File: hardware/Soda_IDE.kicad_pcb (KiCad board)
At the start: 2 copper layers, 101.6 x 65.5 mm, 25 parts, among them CN1 MSX_SLOT_CON, J2 Conn_CF_Card, J3 Conn_02x22_Odd_Even, Q1 BC548, SW1 SW_Push, SW2 SW_Push_SPDT, U1 27C512, U2 74HCT74, U3 74LS32, U4 74HCT138

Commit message: fixes and updates
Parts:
- added JP2: SolderJumper_2_Open, Jumper:SolderJumper-2_P1.3mm_Open_RoundedPad1.0x1.5mm, F.Cu at (186.1, 105.4)
- added JP3: SolderJumper_2_Open, Jumper:SolderJumper-2_P1.3mm_Open_RoundedPad1.0x1.5mm, F.Cu at (190.5, 105.4)
- added JP4: SolderJumper_2_Open, Jumper:SolderJumper-2_P1.3mm_Open_RoundedPad1.0x1.5mm, F.Cu at (194.9, 105.4)
- U2: renamed from U3; value 74LS32 -> 74HCT32
- renumbered C3 to C2, C2 to C3, D2 to D1, J3 to J1, JP2 to J2, J2 to J3, D1 to LD1, R6 to R1, R4 to R2, R5 to R3, R2 to R4, R1 to R5, R3 to R6, U2 to U3
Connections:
- J3 pad 7: /~{SEL} -> /~{IDE_CS0}
- U3 pad 13: /IORQ -> /~{IORQ}
- U4 pad 12: unconnected-(U4-~{Y3}-Pad12) -> Net-(JP2-A)
- U4 pad 13: /~{IDE_CS0} -> Net-(JP3-A)
- U4 pad 15: unconnected-(U4-~{Y0}-Pad15) -> Net-(JP4-A)
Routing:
- net /~{IORQ}: track 0.00 -> 51.4 mm, vias 0 -> 1
- net /~{IDE_CS0}: track 97.2 -> 144.3 mm, vias 1 -> 2
- net Net-(JP4-A): track 0.00 -> 11.5 mm
- net Net-(JP3-A): track 0.00 -> 11.3 mm
- net Net-(JP2-A): track 0.00 -> 10.7 mm
- net /CLOCK: track 100.6 -> 106.2 mm
- net Net-(D1-K): track 64.5 -> 66.6 mm
- net Net-(Q1-B): track 7.30 -> 5.80 mm
- net /D7: track 105.5 -> 106.0 mm
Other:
- board text added: "10h"
- board text added: "30h"
- board text added: "38h"
- board text added: "PCB by Danjovic FW by b3rendsh October 2024"
- board text added: "Z80 RESET"
- board text removed: "Danjovic 2024"

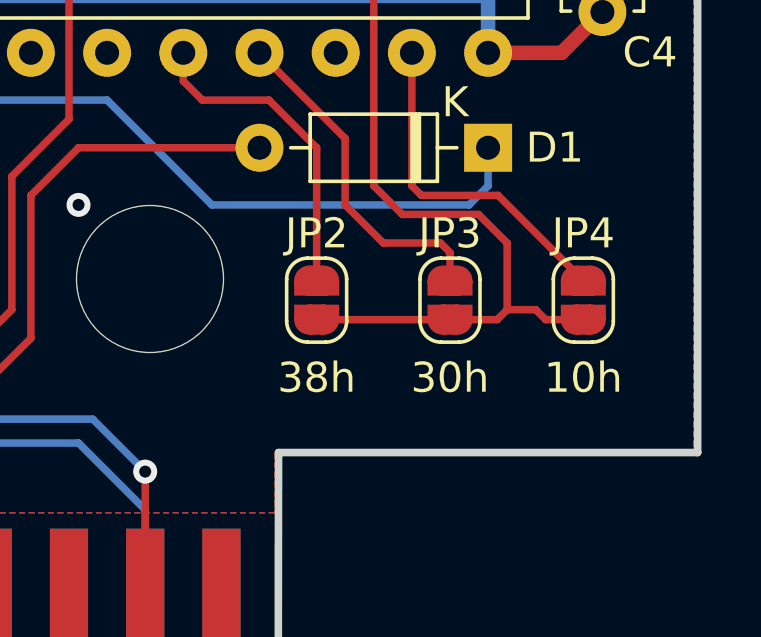
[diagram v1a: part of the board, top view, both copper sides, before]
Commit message: conventional jumpers for address selection
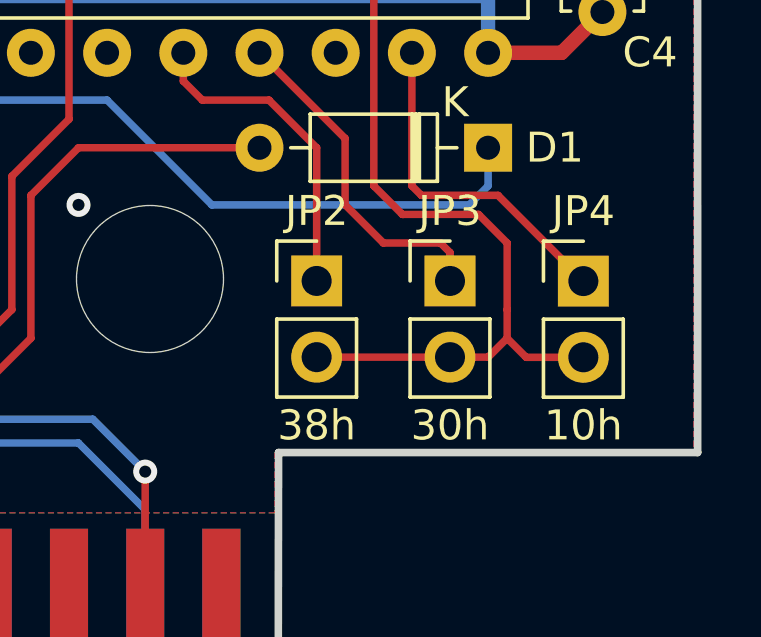
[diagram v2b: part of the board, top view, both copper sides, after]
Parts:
- JP2, JP3, JP4: value SolderJumper_2_Open -> Jumper_2_Small_Open; footprint Jumper:SolderJumper-2_P1.3mm_Open_RoundedPad1.0x1.5mm -> Connector_PinHeader_2.54mm:PinHeader_1x02_P2.54mm_Vertical
- moved JP2 0.64 mm to (186.1, 104.8), turned to 0 degrees
- moved JP3 0.64 mm to (190.5, 104.8), turned to 0 degrees
- moved JP4 0.63 mm to (194.9, 104.8), turned to 0 degrees
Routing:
- net /~{IDE_CS0}: track 144.3 -> 145.5 mm

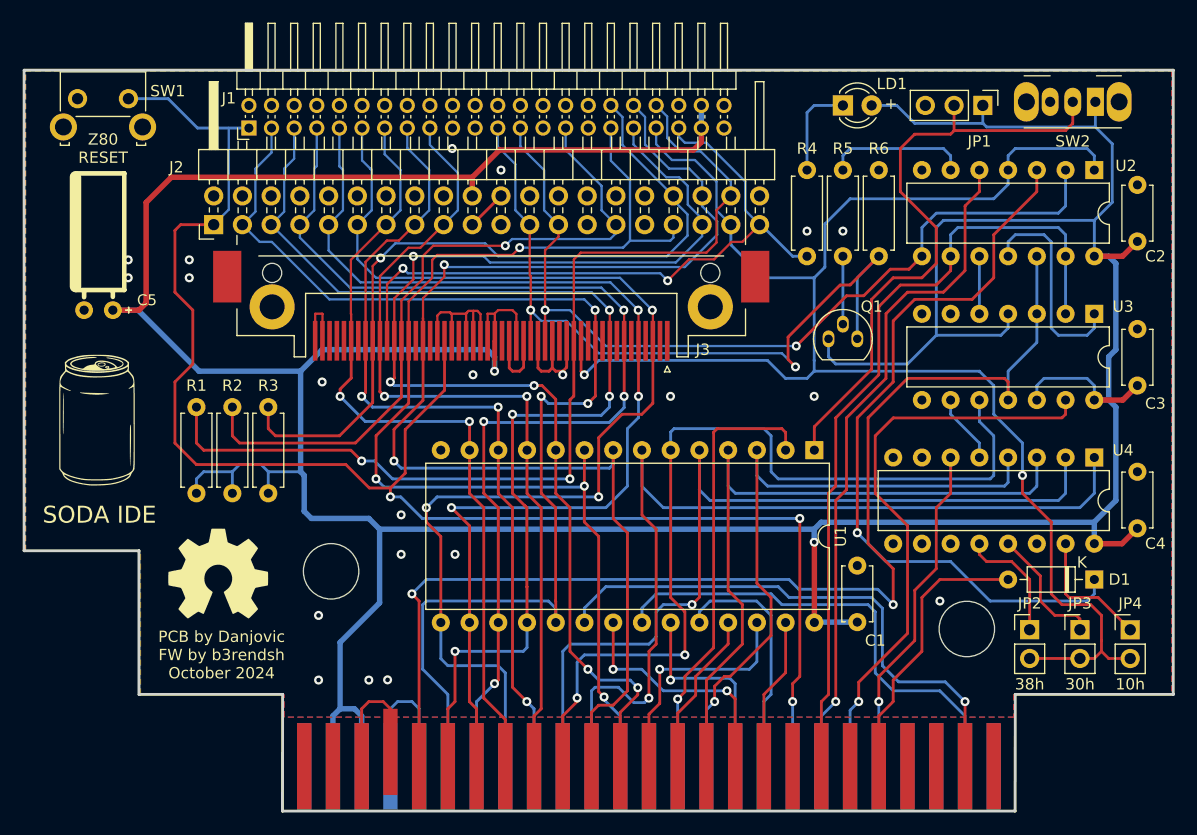
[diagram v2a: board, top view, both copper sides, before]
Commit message: Added buffer to data lines
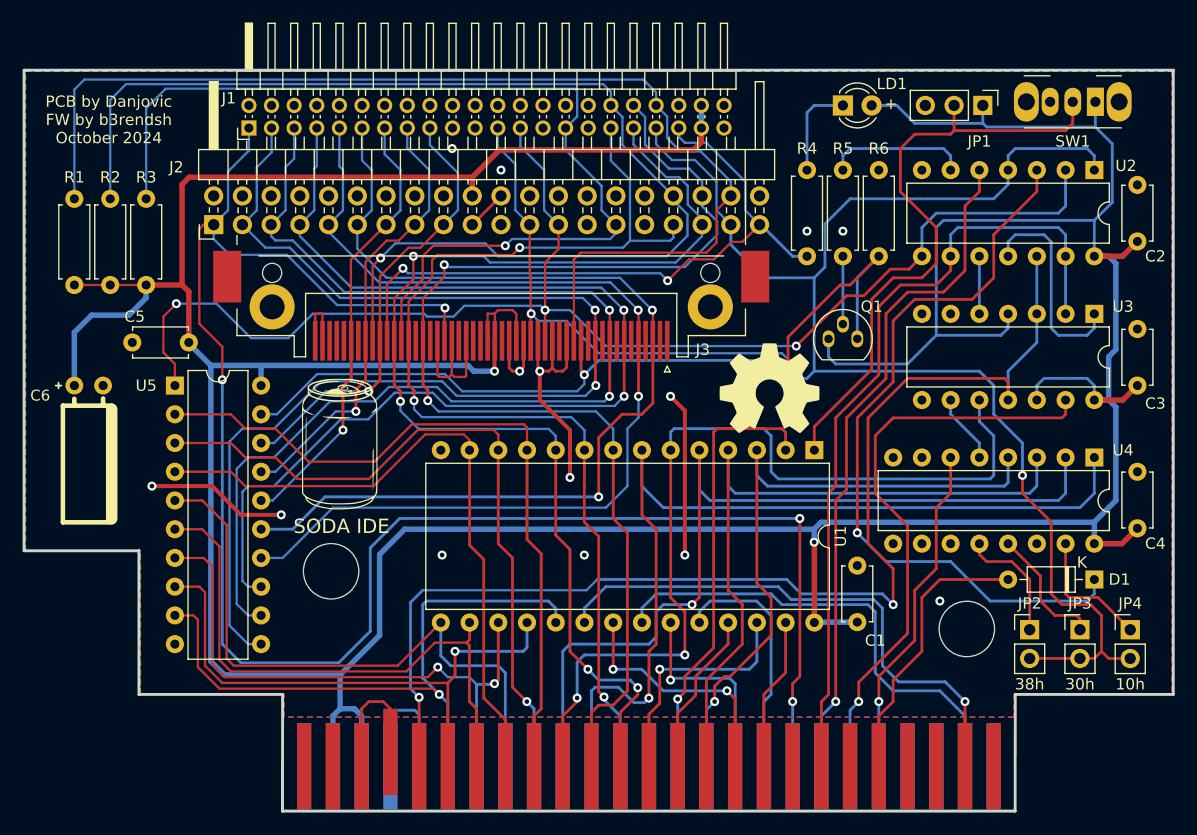
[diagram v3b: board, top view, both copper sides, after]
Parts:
- removed the SW1 at (101.9, 57.8)
- added C5: 100nF, Capacitor_THT:C_Disc_D4.7mm_W2.5mm_P5.00mm, F.Cu at (111.7, 79.4)
- added U5: 74HC245, Package_DIP:DIP-20_W7.62mm, F.Cu at (110.5, 83.2)
- moved R2 23.1 mm to (104.8, 66.7)
- moved R1 21.3 mm to (101.6, 66.7)
- moved R3 19.9 mm to (108.0, 66.7)
- moved C6 6.72 mm to (102.9, 83.2), turned to 0 degrees
- renumbered C5 to C6, R3 to R2, R2 to R3, SW2 to SW1
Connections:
- CN1 pad 33: /D1 -> /zD1
- CN1 pad 34: /D0 -> /zD0
- CN1 pad 35: /D3 -> /zD3
- CN1 pad 36: /D2 -> /zD2
- CN1 pad 37: /D5 -> /zD5
- CN1 pad 38: /D4 -> /zD4
- CN1 pad 39: /D7 -> /zD7
- CN1 pad 40: /D6 -> /zD6
- U1 pad 11: /D0 -> /zD0
- U1 pad 12: /D1 -> /zD1
- U1 pad 13: /D2 -> /zD2
- U1 pad 15: /D3 -> /zD3
- U1 pad 16: /D4 -> /zD4
- U1 pad 17: /D5 -> /zD5
- U1 pad 18: /D6 -> /zD6
- U1 pad 19: /D7 -> /zD7
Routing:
- net /zD0: track 0.00 -> 65.1 mm
- net /zD1: track 0.00 -> 62.5 mm, vias 0 -> 1
- net /zD2: track 0.00 -> 58.8 mm
- net /zD7: track 0.00 -> 57.3 mm, vias 0 -> 1
- net /zD3: track 0.00 -> 55.6 mm
- net /zD5: track 0.00 -> 51.5 mm, vias 0 -> 2
- net /zD4: track 0.00 -> 51.1 mm
- net /zD6: track 0.00 -> 50.6 mm, vias 0 -> 1
- net /~{IORD}: track 77.8 -> 121.4 mm, vias 2 -> 3
- net /PDIAG: track 68.9 -> 105.9 mm
- net /D0: track 74.5 -> 39.6 mm, vias 2 -> 1
- net /D1: track 73.1 -> 39.7 mm, vias 3 -> 1
- net GND: track 55.0 -> 86.9 mm, vias 21 -> 15
- net /~{IDE_CS0}: track 145.5 -> 177.2 mm
- net /D2: track 70.7 -> 39.2 mm, vias 2 -> 1
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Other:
- board text removed: "Z80 RESET"

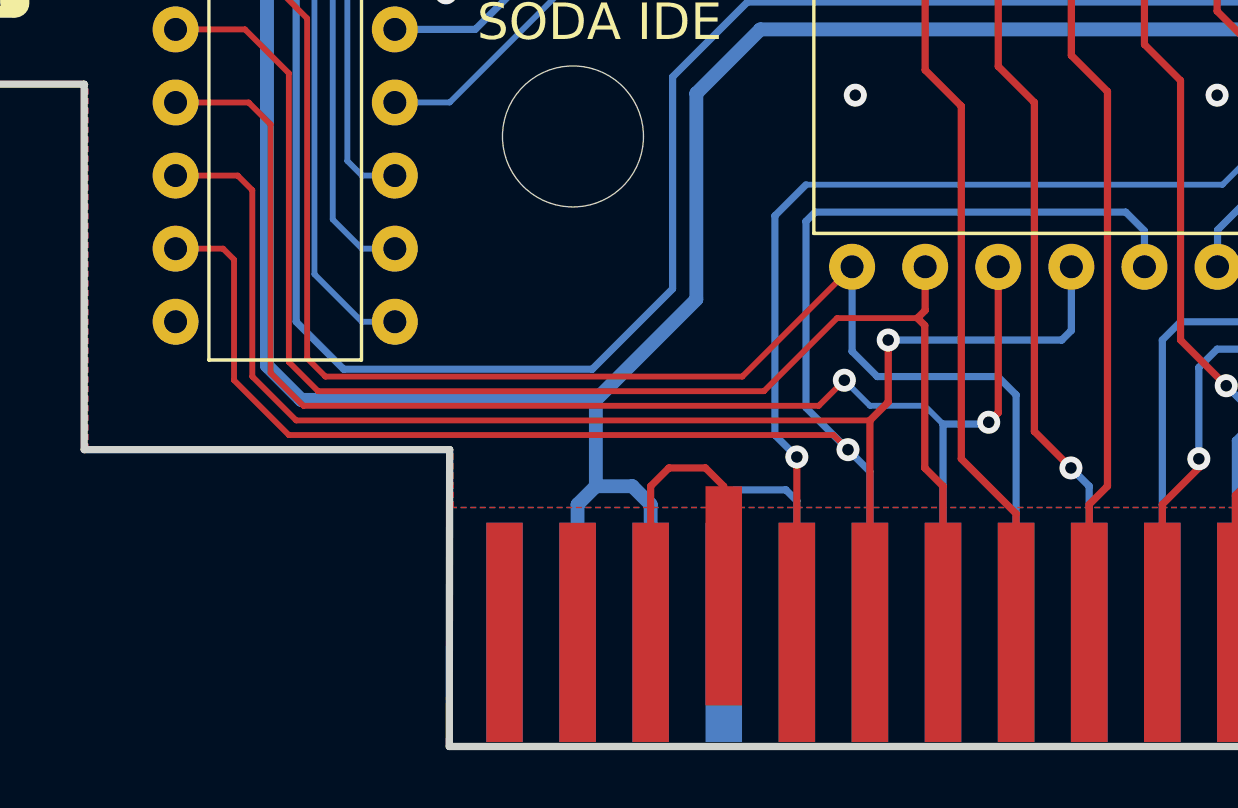
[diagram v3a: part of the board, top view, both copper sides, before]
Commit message: Added buffer to data lines
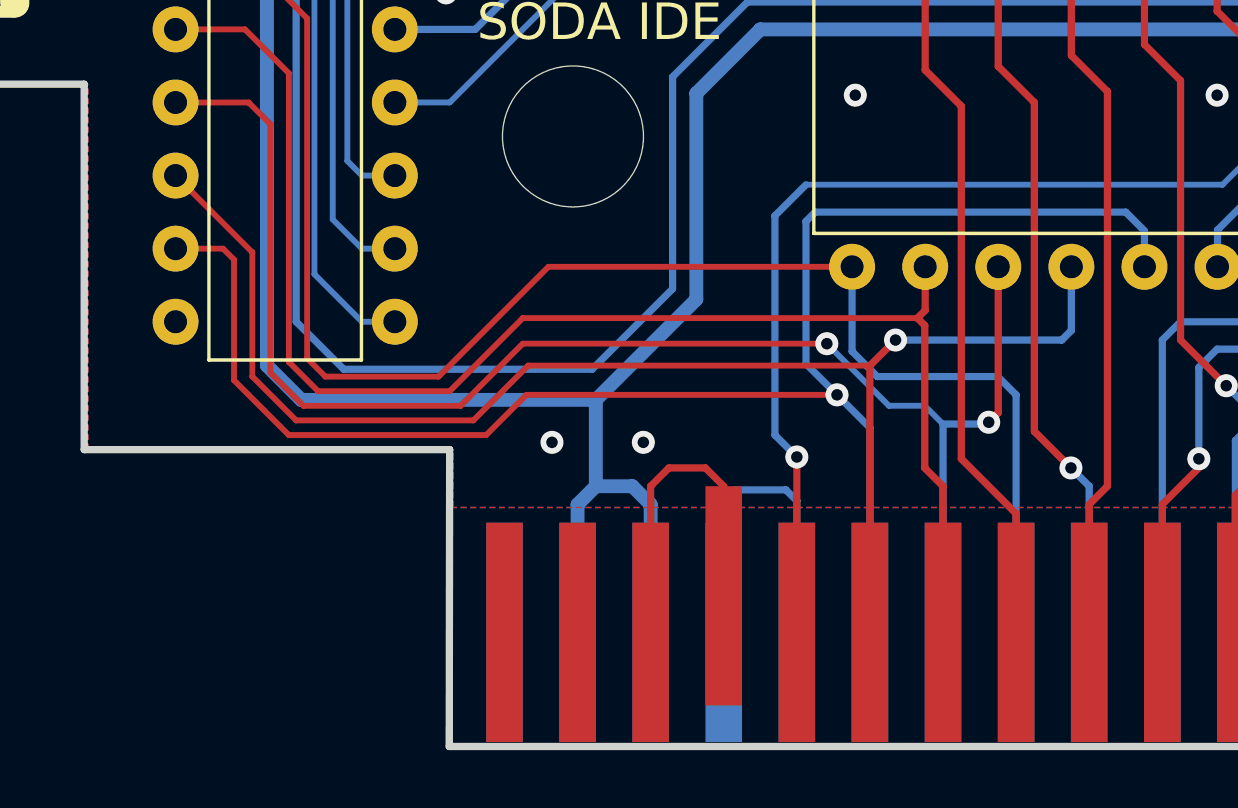
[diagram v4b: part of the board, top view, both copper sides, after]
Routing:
- net /zD5: track 51.5 -> 52.5 mm
- net /zD6: track 50.6 -> 50.0 mm
- net GND: vias 15 -> 17

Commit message: updated board
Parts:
- moved R1 6.35 mm to (101.6, 66.7)
- moved R3 6.35 mm to (108.0, 66.7)
- renumbered R3 to R1, R1 to R3
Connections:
- SW1 pad : (no net) -> GND
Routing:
- net /~{IDE_CS1}: track 99.9 -> 87.2 mm
- net /zD3: track 55.6 -> 45.5 mm
- net /zD4: track 51.1 -> 43.1 mm
- net /zD5: track 52.5 -> 45.7 mm
- net /PDIAG: track 105.9 -> 100.5 mm
- net /zD6: track 50.0 -> 45.9 mm
- net /zD7: track 57.3 -> 53.7 mm
- net /~{DMACK}: track 87.9 -> 84.9 mm
- net GND: track 86.9 -> 89.3 mm, vias 17 -> 18
- net /LED: track 58.5 -> 59.6 mm
- net /~{IDE_CS0}: track 177.2 -> 176.4 mm
